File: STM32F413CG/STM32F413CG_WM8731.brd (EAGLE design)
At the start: 54 x 33 mm, 59 parts, among them IC1 STM32F413CGU6, IC2 WM8731SEDS_RV, J2 1503_02, X1 USB-MICROB-SMD

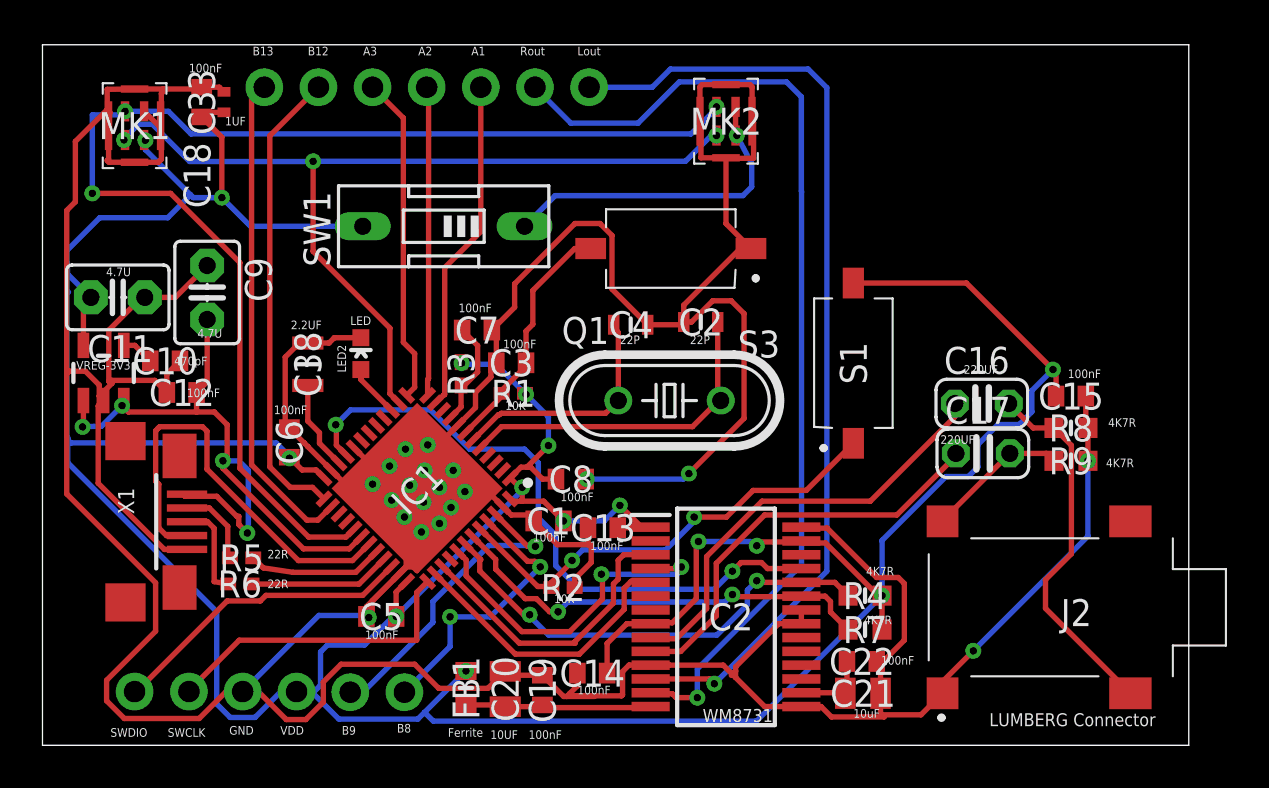
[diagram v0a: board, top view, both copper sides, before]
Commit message: adjusted some smd components
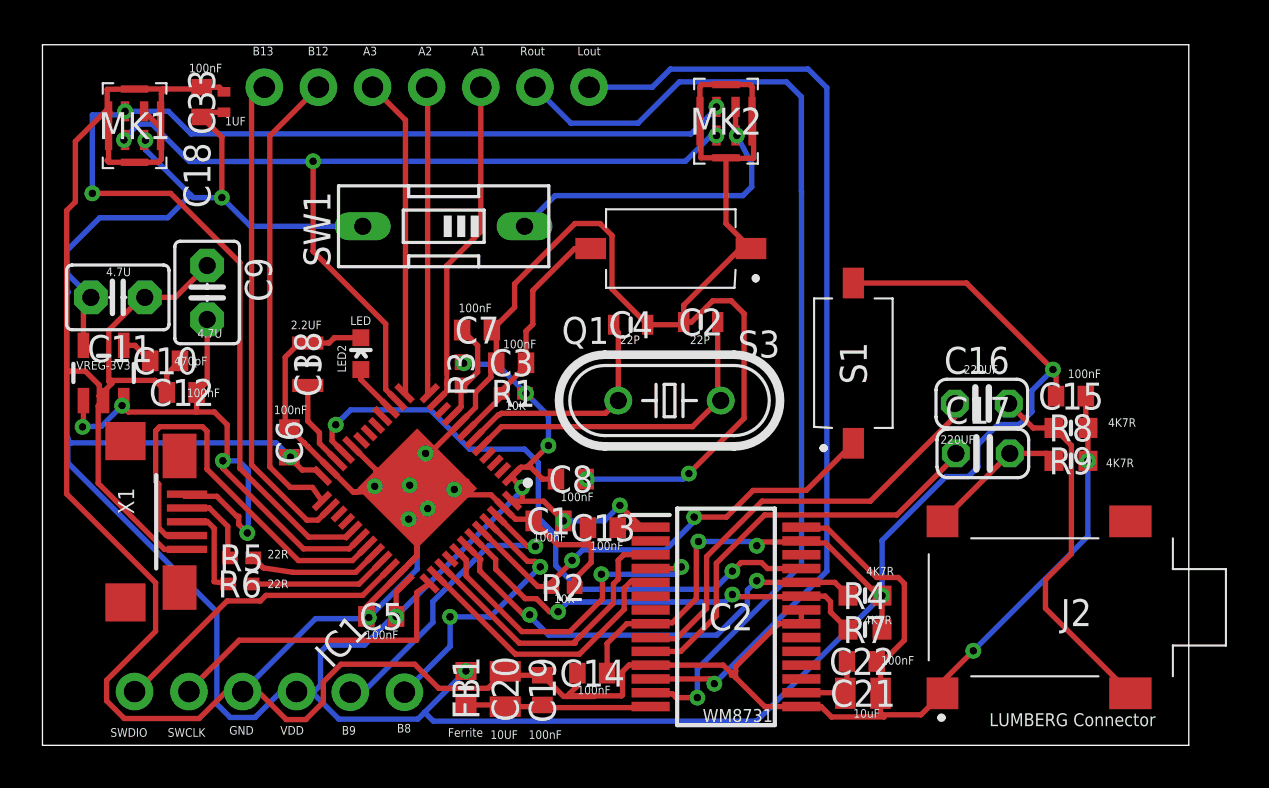
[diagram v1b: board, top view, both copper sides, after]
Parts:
- IC1: device STM32F413CGU6:QFN50P700X700X60-49N -> STM32F413CG_edited:QFN50P700X700X60-49N
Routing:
- net GND: track 277.8 -> 340.4 mm, vias 5 -> 11
- net VDD: track 192.3 -> 191.5 mm
- net B13: track 22.9 -> 23.5 mm
- added copper zone on layer 16, net GNG
- removed copper zone on layer 16, net HEAT2
